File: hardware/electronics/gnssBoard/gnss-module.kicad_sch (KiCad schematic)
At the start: 29 parts, among them Q5 DMG1013TQ-7, U2 ZED-F9P, U3 OPA344, U4 TXS0104VxRUTR

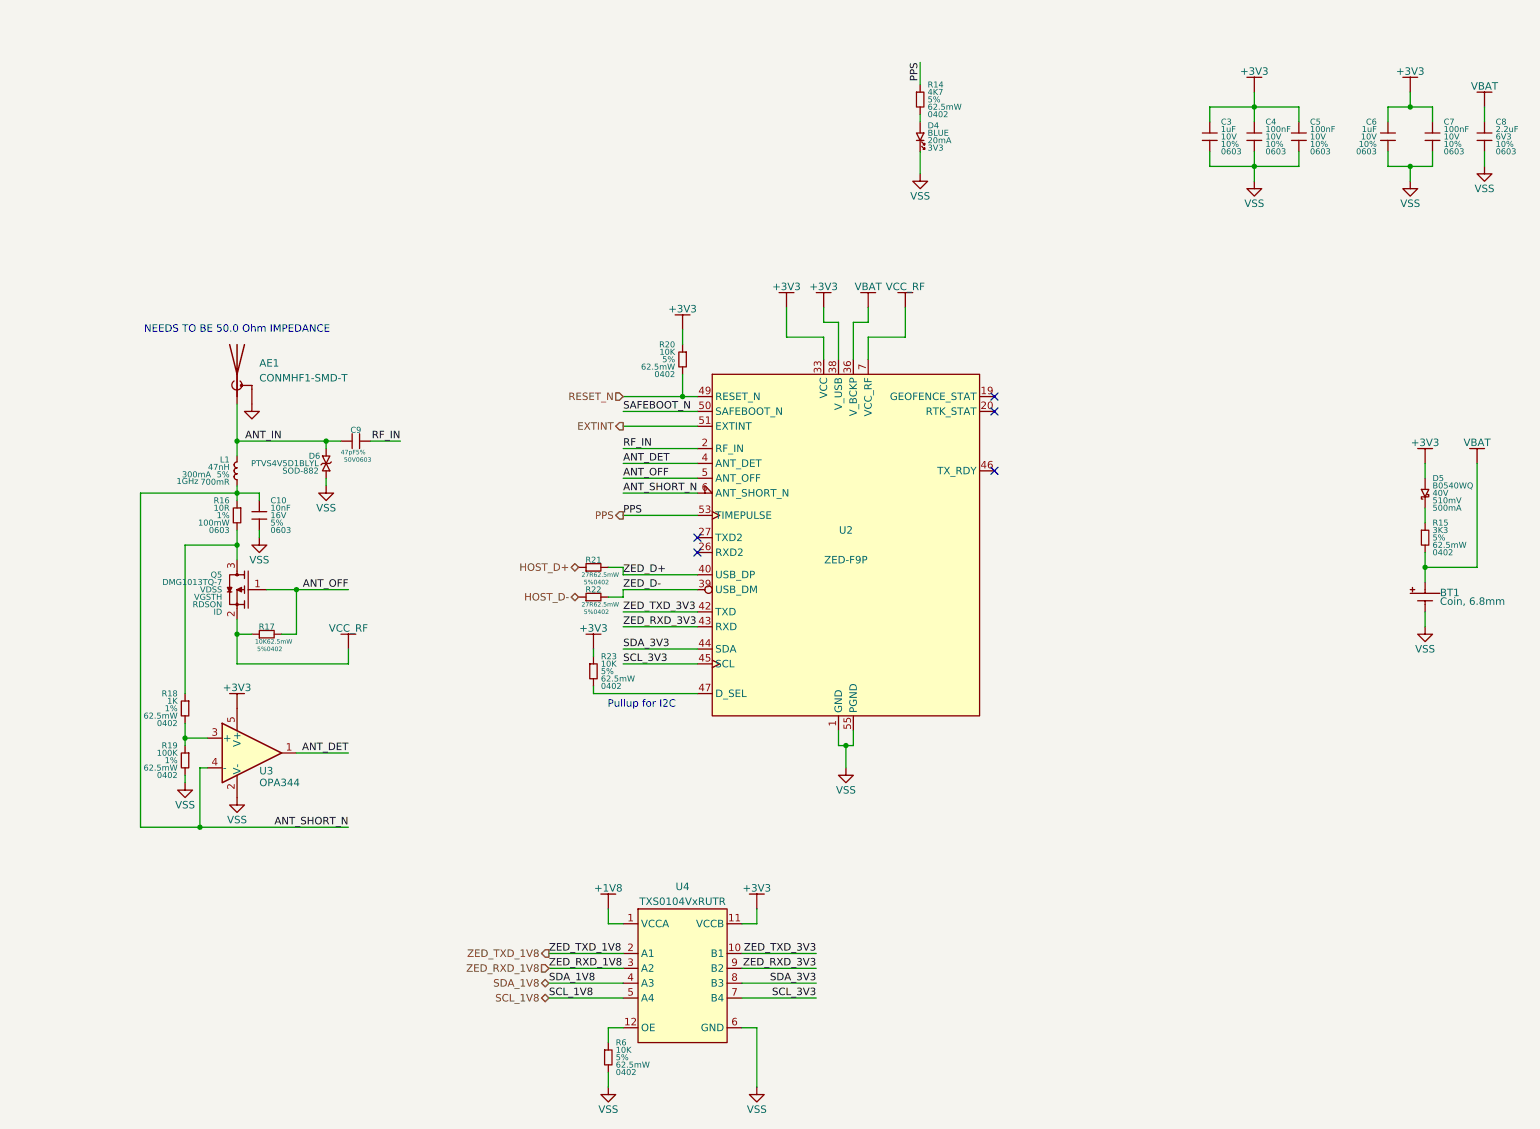
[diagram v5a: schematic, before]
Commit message: re-added cut traces and test points and flxed keepout for edge connector
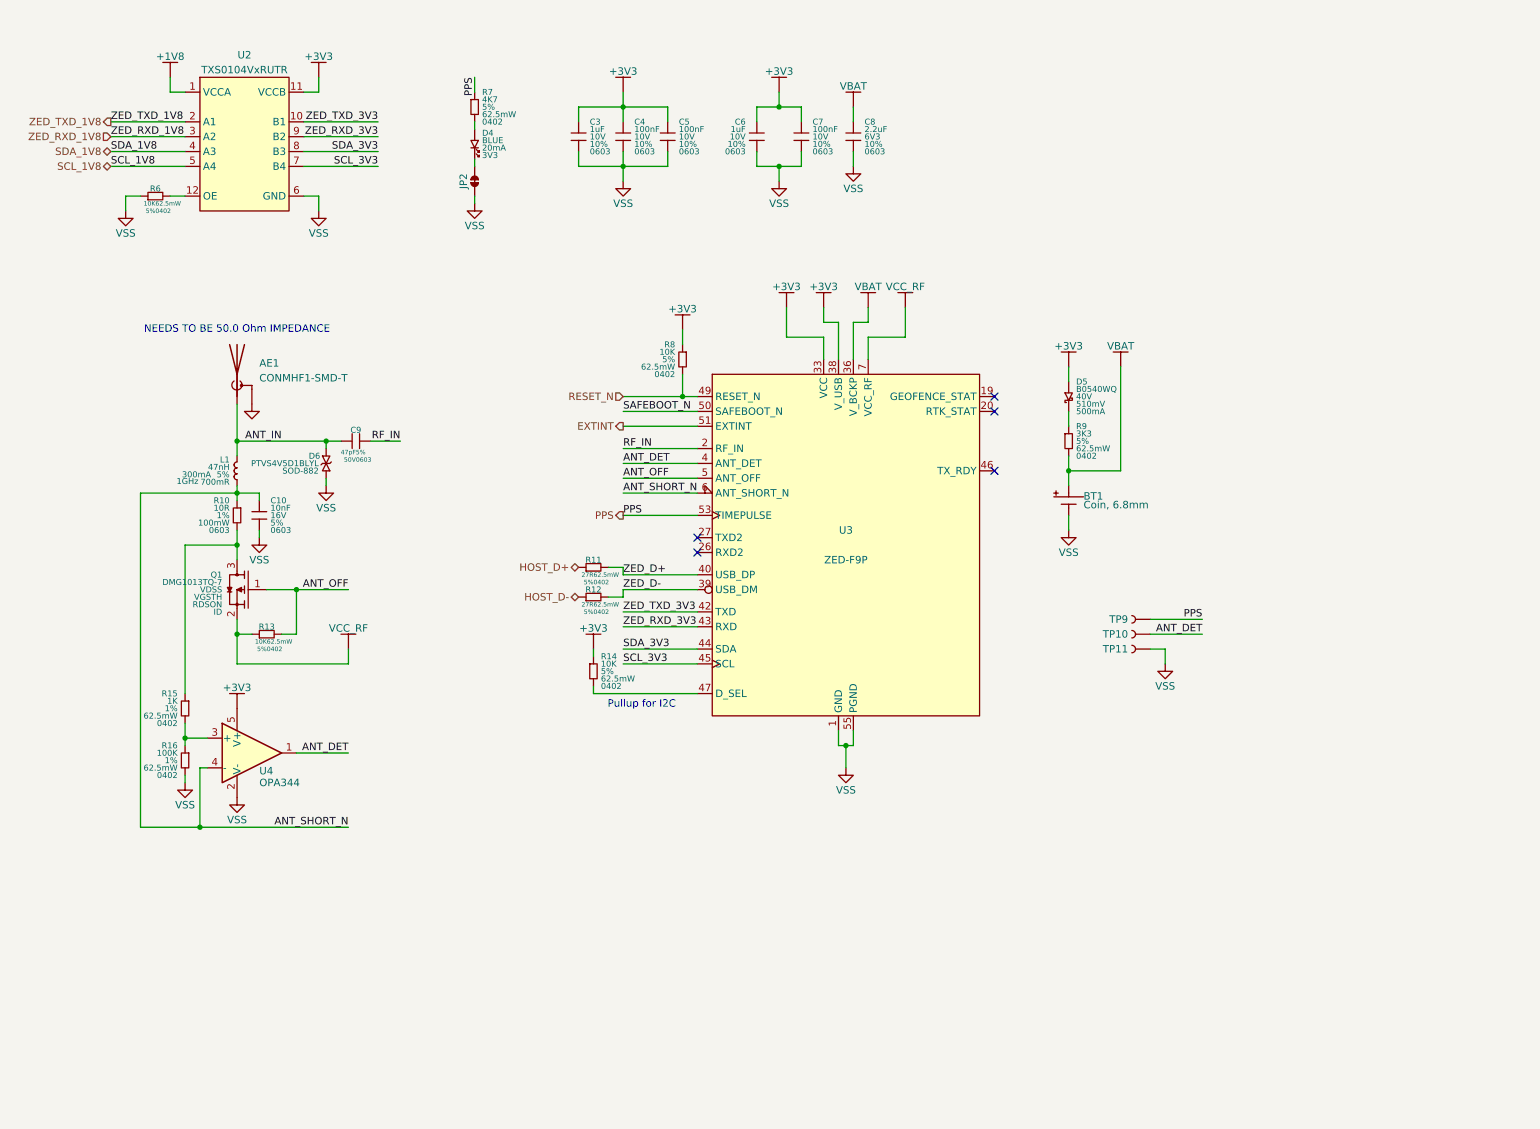
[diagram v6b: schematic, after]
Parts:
- removed R6: 10K, lib_fp:CRCW0402, symbol lib_sch:R
- added JP2: ~, lib_fp:Jumper_2_Bridged, symbol lib_sch:Jumper_2_Bridged
- added R6: 10K, lib_fp:CRCW0402, symbol lib_sch:R_horizontal
- added TP10, TP11, TP9: ~, lib_fp:TP_1mm, symbol lib_sch:Testpoint
- renumbered Q5 to Q1, R16 to R10, R21 to R11, R22 to R12, R17 to R13, R23 to R14, R18 to R15, R19 to R16, R14 to R7, R20 to R8, R15 to R9, U4 to U2, U2 to U3, U3 to U4
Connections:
- net ANT_DET: now also TP10.1
- net PPS: now also TP9.1
- net VSS: now also JP2.2, R6.1, TP11.1; no longer D4.2
- net at U2.12 (OE): now also R6.2
- new net: D4.2, JP2.1
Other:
- title: (none) -> GNSS Module
- moved on the sheet: BT1, C3, C4, C5, C6, C7, C8, D4, D5, R7, R9, U2

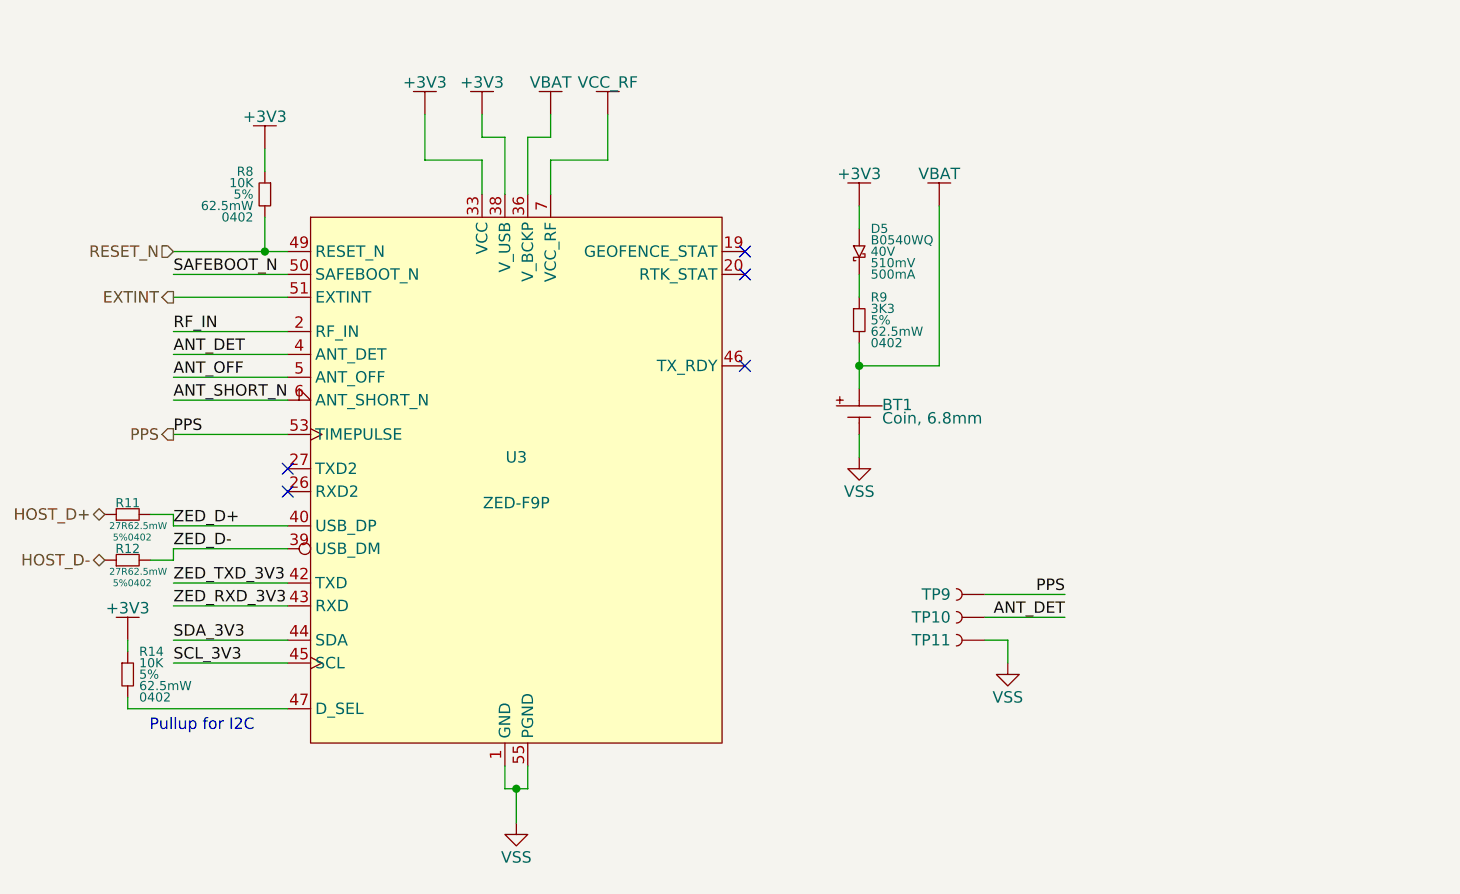
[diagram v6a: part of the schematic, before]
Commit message: moved around vendor defined signals and reset line
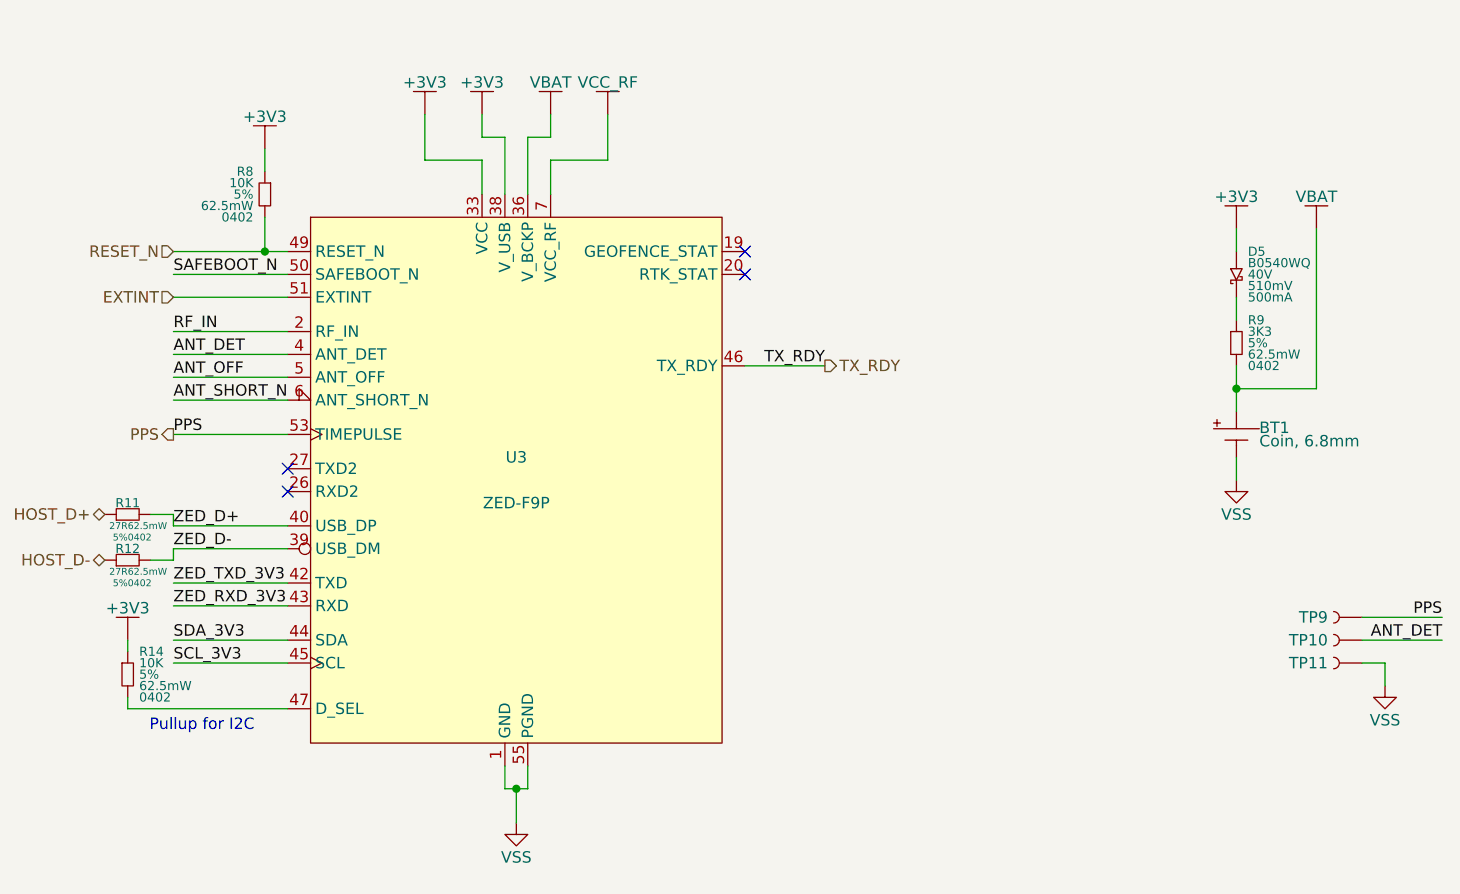
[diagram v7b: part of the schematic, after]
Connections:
- net TX_RDY: now reaches U3.46 (TX_RDY)
- no-connect marks 5 -> 4
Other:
- moved on the sheet: BT1, D5, R9, TP10, TP11, TP9
